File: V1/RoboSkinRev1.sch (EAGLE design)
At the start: 10 parts, among them U4 LSM6DS3DOT_INDICATION, U5 VL53L1XSMD

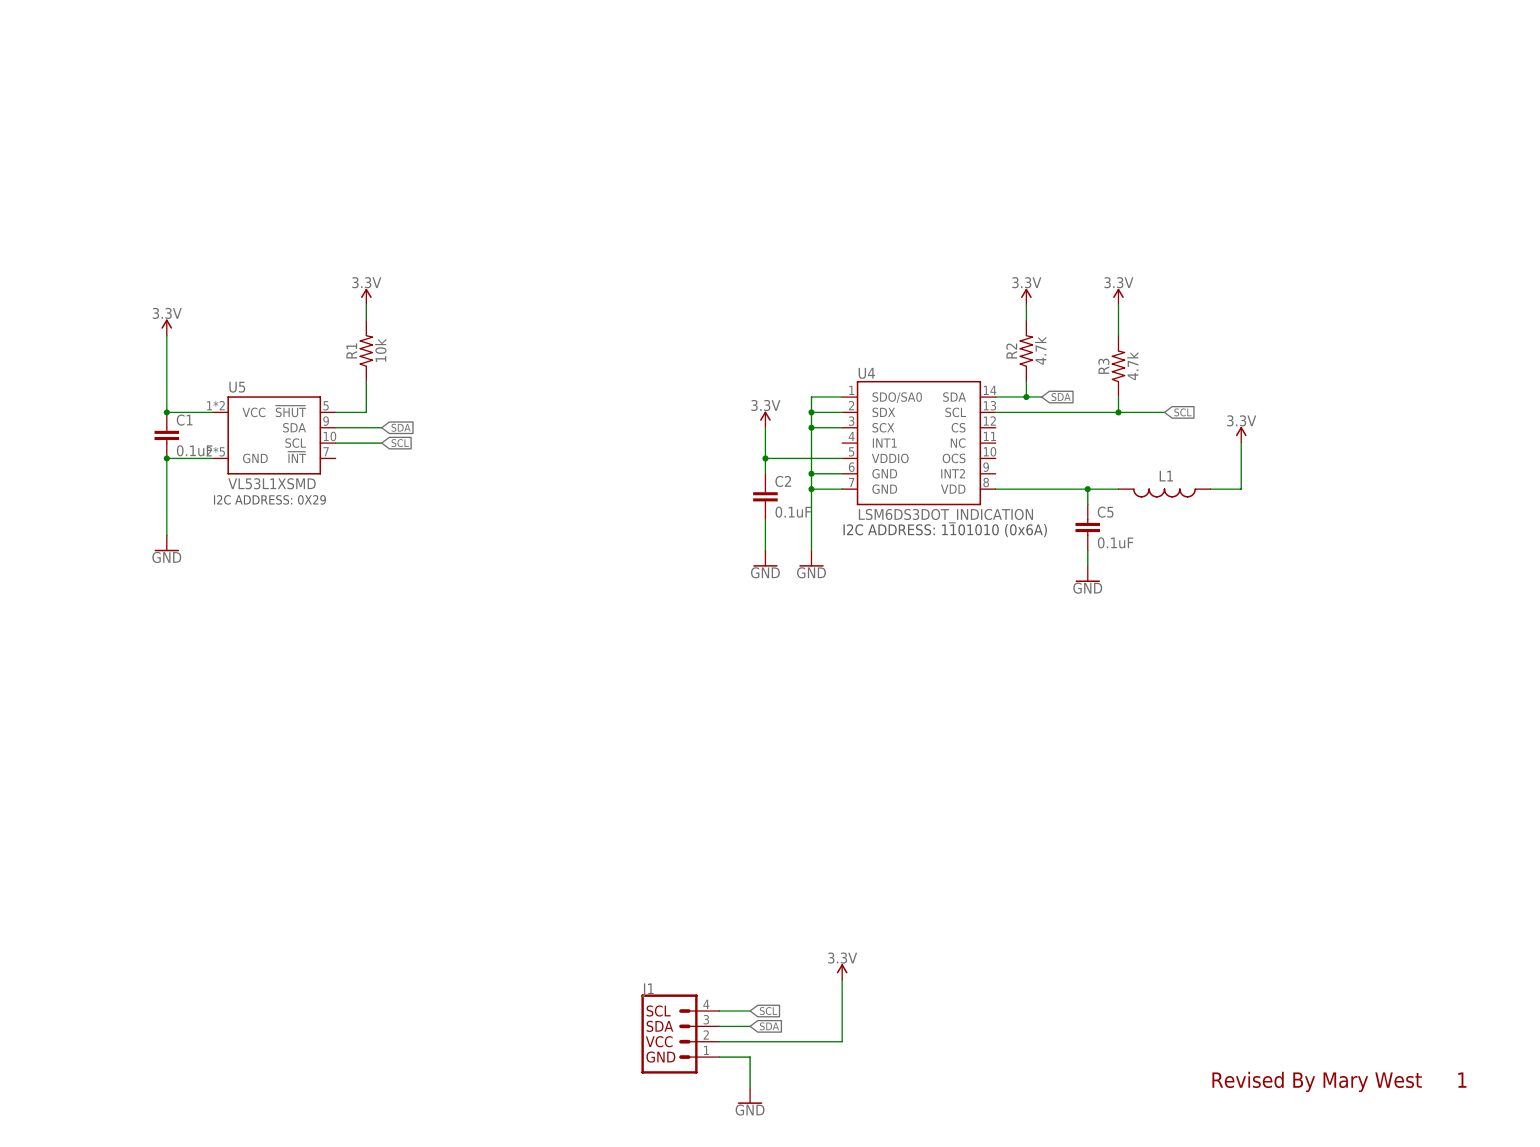
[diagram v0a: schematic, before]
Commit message: Updated schematics with new sensors and supporting circuitry
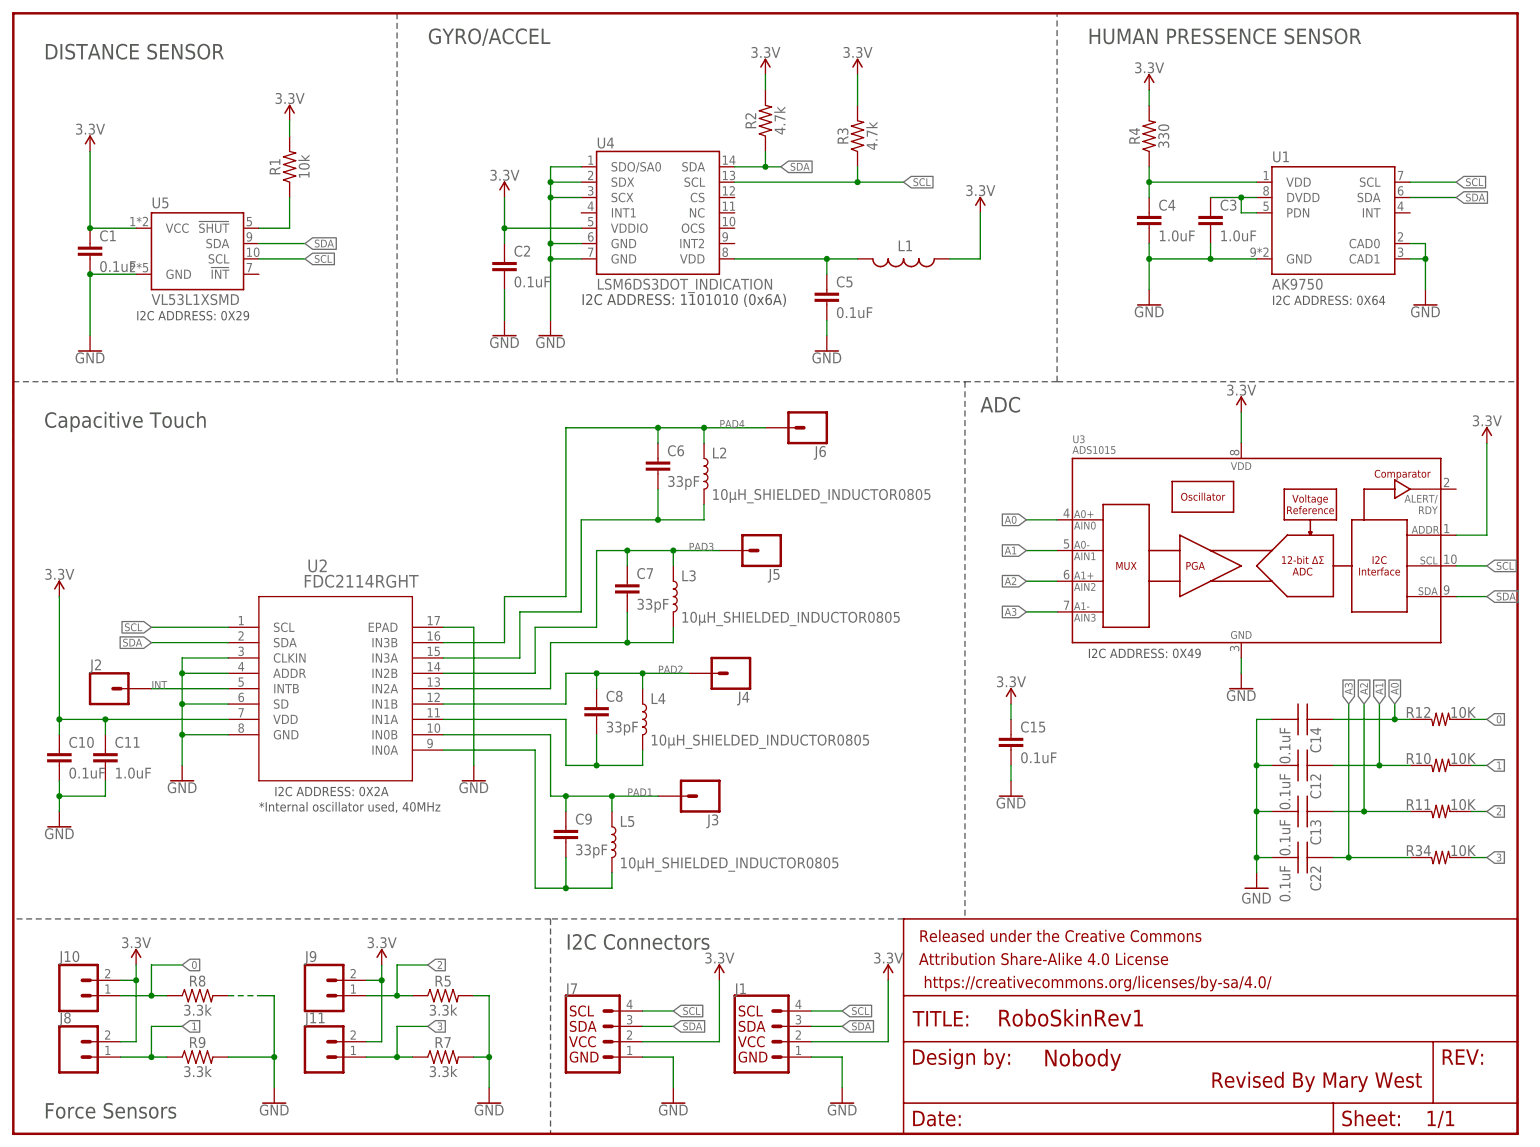
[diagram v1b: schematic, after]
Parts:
- added C10, C15: 0.1uF, SparkFun-Capacitors:0.1UF-0603-25V-(+80/-20%)
- added C11, C3, C4: 1.0uF, SparkFun-Capacitors:1.0UF-0603-16V-10%
- added C12, C13, C14, C22: 0.1uF, 1_BES_Passives:CAPACITORC_0603_SILK
- added C6, C7, C8, C9: 33pF, SparkFun-Capacitors:33PF-0603-50V-5%
- added FRAME1: FRAME-LETTERNO_PACKAGE, SparkFun-Aesthetics:FRAME-LETTERNO_PACKAGE
- added J10, J11, J8, J9: (no value), SparkFun-Connectors:CONN_02
- added J2, J3, J4, J5, J6: (no value), SparkFun-Connectors:CONN_01
- added J7: (no value), SparkFun-Connectors:QWIIC_CONNECTORJS-1MM
- added L2, L3, L4, L5: 10μH_SHIELDED_INDUCTOR0805, SparkFun-Coils:10μH_SHIELDED_INDUCTOR0805
- added R10, R11, R12, R34: 10K, 1_BES_Passives:RESISTORR_0603_SILK
- added R4: 330, SparkFun-Resistors:330OHM-0603-1/10W-1%
- added R5, R7, R8, R9: 3.3k, SparkFun-Resistors:3.3KOHM-0603-1/10W-1%
- added U1: AK9750, SparkFun-Sensors:AK9750
- added U2: FDC2114RGHT, FDC2114:FDC2114RGHT
- added U3: ADS1015, SparkFun-IC-Conversion:ADS1015
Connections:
- new net 0: J10.1, R12.2, R8.1
- new net 1: J8.1, R10.2, R9.1
- new net 2: J9.1, R11.2, R5.1
- new net 3: J11.1, R34.2, R7.1
- new net A0: C14.1, R12.1, U3.AIN0
- new net A1: C12.1, R10.1, U3.AIN1
- new net A2: C13.1, R11.1, U3.AIN2
- new net A3: C22.1, R34.1, U3.AIN3
- new net INT: J2.1, U2.INTB
- new net N$1: C4.1, R4.1, U1.VDD
- new net N$10: C7.2, L3.2, U2.IN2A
- new net N$12: C8.2, L4.2, U2.IN1A
- new net N$14: C9.2, L5.2, U2.IN0A
- new net N$2: C3.1, U1.DVDD, U1.PDN
- new net N$8: C6.2, L2.2, U2.IN3A
- new net PAD1: C9.1, J3.1, L5.1, U2.IN0B
- new net PAD2: C8.1, J4.1, L4.1, U2.IN1B
- new net PAD3: C7.1, J5.1, L3.1, U2.IN2B
- new net PAD4: C6.1, J6.1, L2.1, U2.IN3B
- net 3.3V: now also C10.1, C11.1, C15.1, J10.2, J11.2, J7.VCC, J8.2, J9.2, R4.2, U2.VDD, U3.ADDR, U3.VDD
- net GND: now also C10.2, C11.2, C12.2, C13.2, C14.2, C15.2, C22.2, C3.2, C4.2, J7.GND, R5.2, R7.2, R8.2, R9.2, U1.CAD0, U1.CAD1, U1.GND, U2.ADDR, U2.CLKIN, U2.EPAD, U2.GND, U2.SD, U3.VSS
- net SCL: now also J7.SCL, U1.SCL, U2.SCL, U3.SCL
- net SDA: now also J7.SDA, U1.SDA, U2.SDA, U3.SDA
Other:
- note added: "*Internal oscillator used, 40MHz"
- note added: "ADC"
- note added: "Capacitive Touch"
- note added: "DISTANCE SENSOR"
- note added: "Force Sensors"
- note added: "GYRO/ACCEL"
- note added: "HUMAN PRESSENCE SENSOR"
- note added: "I2C ADDRESS: 0X2A"
- note added: "I2C ADDRESS: 0X49"
- note added: "I2C ADDRESS: 0X64"
- note added: "I2C Connectors"
- note removed: "1"
- moved on the sheet: C1, C2, C5, J1, L1, R1, R2, R3, U4, U5
